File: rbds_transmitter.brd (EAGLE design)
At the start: 80 x 75.9 mm, 136 parts, among them J1 AVRISP-6, Q1 P-Ch, Q2 P-Ch, Q3 P-CH, T1 ATB3225-75032CT, T2 ATB3225-75032CT, U1 MAX2606, U2 TS974, U3 TS974, U4 MCP4812, U5 ATMEGA328, U6 MAX1551, U7 TPS61030, X1 16Mhz

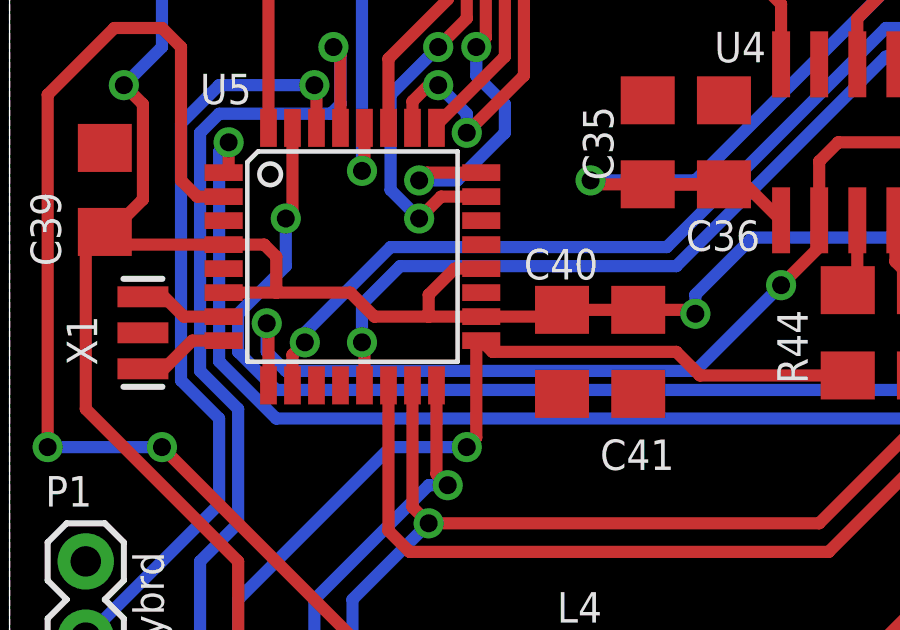
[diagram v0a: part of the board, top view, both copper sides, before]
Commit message: engineering change request form: swapped pd6 and pb1
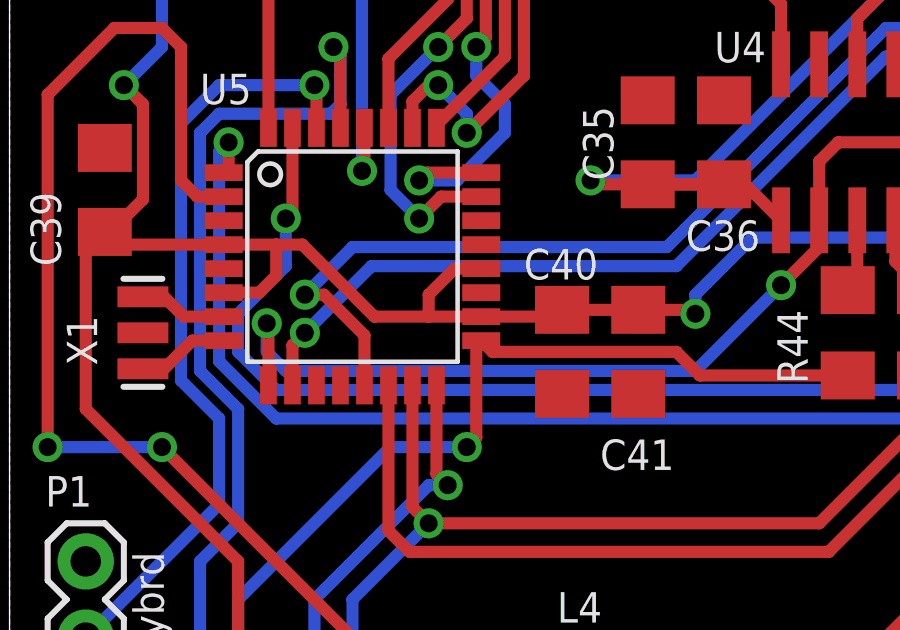
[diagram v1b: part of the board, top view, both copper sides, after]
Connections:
- net !DAC_LATCH: now also U5.13; no longer U5.10
- net CARRIER: now also U5.10; no longer U5.13
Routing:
- net !DAC_LATCH: track 35.9 -> 37.7 mm
- net CARRIER: track 90.4 -> 91.9 mm
- net +5V: track 216.2 -> 216.7 mm
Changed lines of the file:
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@@
 <wire x1="15.7226" y1="23.4" x2="13.97" y2="23.4" width="0.4064" layer="1"/>
 <wire x1="13.97" y1="23.4" x2="12.16" y2="23.4" width="0.4064" layer="1"/>
-<wire x1="12.16" y1="23.4" x2="11.36" y2="24.2" width="0.4064" layer="1"/>
-<wire x1="7.1374" y1="24.2" x2="8.89" y2="24.2" width="0.4064" layer="1"/>
-<wire x1="8.89" y1="24.2" x2="11.36" y2="24.2" width="0.4064" layer="1"/>
-<wire x1="7.1374" y1="25.8" x2="8.49" y2="25.8" width="0.4064" layer="1"/>
-<wire x1="8.49" y1="25.8" x2="8.89" y2="25.4" width="0.4064" layer="1"/>
-<wire x1="8.89" y1="25.4" x2="8.89" y2="24.2" width="0.4064" layer="1"/>
+<wire x1="7.1374" y1="25.8" x2="8.89" y2="25.8" width="0.4064" layer="1"/>
+<wire x1="8.89" y1="25.8" x2="9.76" y2="25.8" width="0.4064" layer="1"/>
 <wire x1="15.7226" y1="25" x2="14.84" y2="25" width="0.4064" layer="1"/>
 <wire x1="14.84" y1="25" x2="13.97" y2="24.13" width="0.4064" layer="1"/>
@@
 <wire x1="73.3425" y1="39.0525" x2="73.3425" y2="21.7325" width="0.4064" layer="1"/>
 <wire x1="73.3425" y1="21.7325" x2="70.66" y2="19.05" width="0.4064" layer="1"/>
+<wire x1="9.76" y1="25.8" x2="12.16" y2="23.4" width="0.4064" layer="1"/>
+<wire x1="7.1374" y1="24.2" x2="8.325" y2="24.2" width="0.4064" layer="1"/>
+<wire x1="8.325" y1="24.2" x2="8.89" y2="24.765" width="0.4064" layer="1"/>
+<wire x1="8.89" y1="24.765" x2="8.89" y2="25.8" width="0.4064" layer="1"/>
 </signal>
 <signal name="ISP-MISO">
@@
 <contactref element="U4" pad="5"/>
 <contactref element="R43" pad="1"/>
-<contactref element="U5" pad="10"/>
 <wire x1="29.5275" y1="31.81" x2="29.5275" y2="32.385" width="0.4064" layer="1"/>
 <wire x1="29.5275" y1="32.385" x2="30.1625" y2="33.02" width="0.4064" layer="1"/>
@@
 <wire x1="32.7025" y1="33.02" x2="33.9725" y2="31.75" width="0.4064" layer="1"/>
 <wire x1="33.9725" y1="31.75" x2="33.9725" y2="30.632" width="0.4064" layer="1"/>
-<via x="9.8425" y="22.5425" extent="1-16" drill="0.6"/>
-<wire x1="12.7" y1="25.7175" x2="21.9075" y2="25.7175" width="0.4064" layer="16"/>
+<via x="9.8425" y="24.13" extent="1-16" drill="0.6"/>
+<wire x1="11.43" y1="25.7175" x2="21.9075" y2="25.7175" width="0.4064" layer="16"/>
 <wire x1="21.9075" y1="25.7175" x2="29.21" y2="33.02" width="0.4064" layer="16"/>
 <wire x1="29.21" y1="33.02" x2="32.7025" y2="33.02" width="0.4064" layer="16"/>
 <via x="32.7025" y="33.02" extent="1-16" drill="0.6"/>
-<wire x1="9.43" y1="21.1074" x2="9.43" y2="22.13" width="0.4064" layer="1"/>
-<wire x1="9.43" y1="22.13" x2="9.8425" y2="22.5425" width="0.4064" layer="1"/>
-<wire x1="12.7" y1="25.7175" x2="9.8425" y2="22.86" width="0.4064" layer="16"/>
-<wire x1="9.8425" y1="22.86" x2="9.8425" y2="22.5425" width="0.4064" layer="16"/>
+<contactref element="U5" pad="13"/>
+<wire x1="11.43" y1="25.7175" x2="9.8425" y2="24.13" width="0.4064" layer="16"/>
+<wire x1="9.8425" y1="24.13" x2="10.4775" y2="24.13" width="0.4064" layer="1"/>
+<wire x1="10.4775" y1="24.13" x2="11.83" y2="22.7775" width="0.4064" layer="1"/>
+<wire x1="11.83" y1="21.1074" x2="11.83" y2="22.7775" width="0.4064" layer="1"/>
 </signal>
 <signal name="!DAC_CS">
@@
 <signal name="CARRIER">
 <contactref element="R23" pad="2"/>
-<contactref element="U5" pad="13"/>
 <wire x1="62.078" y1="49.53" x2="62.078" y2="49.378" width="0.4064" layer="1"/>
 <wire x1="62.078" y1="49.378" x2="60.6425" y2="47.9425" width="0.4064" layer="1"/>
@@
 <wire x1="60.6425" y1="46.0375" x2="61.2775" y2="45.4025" width="0.4064" layer="1"/>
 <wire x1="61.2775" y1="45.4025" x2="71.4375" y2="45.4025" width="0.4064" layer="1"/>
-<wire x1="11.83" y1="21.1074" x2="11.83" y2="22.46" width="0.4064" layer="1"/>
-<wire x1="11.83" y1="22.46" x2="11.7475" y2="22.5425" width="0.4064" layer="1"/>
-<via x="11.7475" y="22.5425" extent="1-16" drill="0.6"/>
-<wire x1="11.7475" y1="22.5425" x2="11.7475" y2="23.8125" width="0.4064" layer="16"/>
-<wire x1="11.7475" y1="23.8125" x2="13.0175" y2="25.0825" width="0.4064" layer="16"/>
-<wire x1="13.0175" y1="25.0825" x2="22.225" y2="25.0825" width="0.4064" layer="16"/>
+<via x="9.8425" y="22.86" extent="1-16" drill="0.6"/>
+<wire x1="12.065" y1="25.0825" x2="22.225" y2="25.0825" width="0.4064" layer="16"/>
 <wire x1="22.225" y1="25.0825" x2="29.21" y2="32.0675" width="0.4064" layer="16"/>
 <wire x1="60.0075" y1="32.0675" x2="71.4375" y2="43.4975" width="0.4064" layer="16"/>
@@
 <wire x1="47.3075" y1="34.6075" x2="46.6725" y2="35.2425" width="0.4064" layer="16"/>
 <wire x1="46.6725" y1="35.2425" x2="42.8625" y2="35.2425" width="0.4064" layer="16"/>
+<contactref element="U5" pad="10"/>
+<wire x1="12.065" y1="25.0825" x2="9.8425" y2="22.86" width="0.4064" layer="16"/>
+<wire x1="9.43" y1="21.1074" x2="9.43" y2="22.4475" width="0.4064" layer="1"/>
+<wire x1="9.43" y1="22.4475" x2="9.8425" y2="22.86" width="0.4064" layer="1"/>
 </signal>
 <signal name="N$10">
